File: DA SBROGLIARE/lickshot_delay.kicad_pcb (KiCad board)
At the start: 2 copper layers, 76 parts, among them Q1 2N3904, SW1 SW_DPDT_x2, SW2 SW_DPDT_x2, U1 4069, U2 4046, U3 TL072, U4 L7805, U5 PT2399

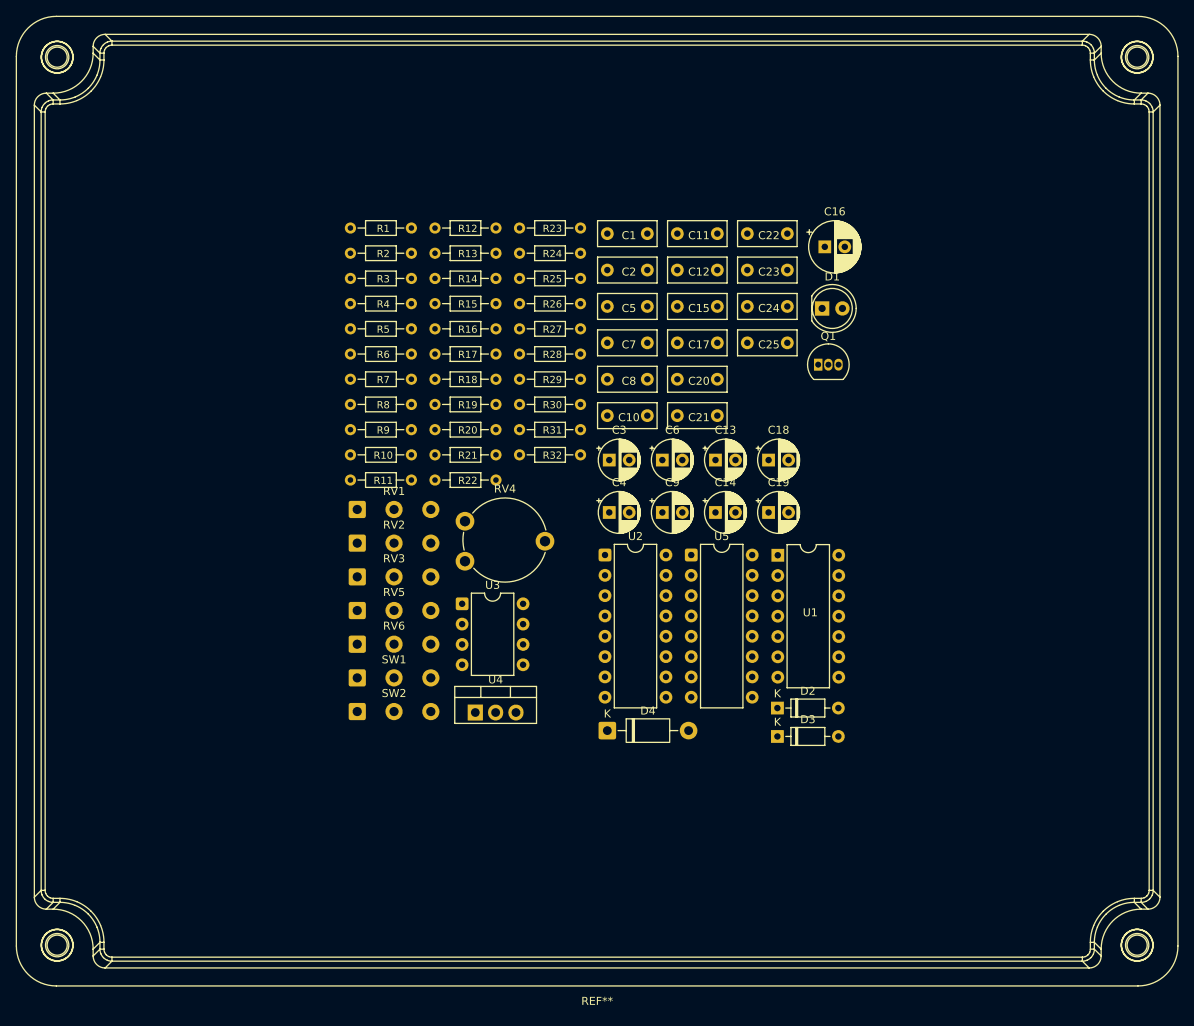
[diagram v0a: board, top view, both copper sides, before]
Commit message: Sbrogliato un po', ho messo i componenti vicino ai IC rispettivi (non ho finito)
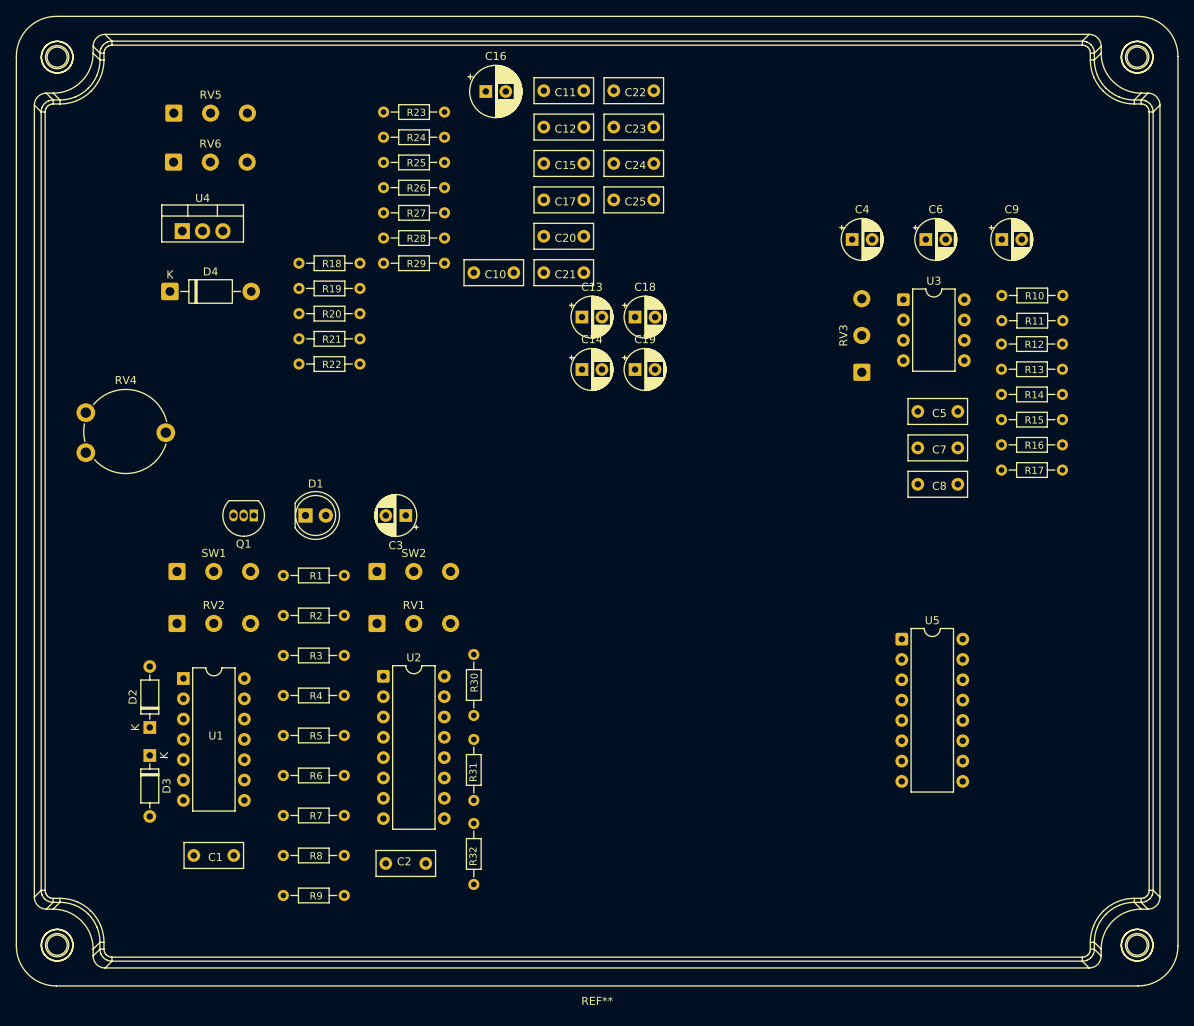
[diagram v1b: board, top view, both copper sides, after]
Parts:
- moved C1 93.3 mm to (71.5, 137.0)
- moved R10 83.8 mm to (172.5, 67.0)
- moved R11 83.8 mm to (172.5, 70.2)
- moved D2 78.5 mm to (66.0, 121.0), turned to 90 degrees
- moved D3 78.5 mm to (66.0, 124.5), turned to -90 degrees
- moved C2 77.6 mm to (100.5, 138.0), turned to 180 degrees
- moved D4 77.5 mm to (68.5, 66.5)
- moved U1 75.9 mm to (70.2, 114.9)
- moved Q1 73.0 mm to (79.0, 94.5), turned to 180 degrees
- moved R12 72.3 mm to (172.5, 73.1)
- moved R13 72.3 mm to (172.5, 76.2)
- moved R14 72.3 mm to (172.5, 79.4)
- moved R15 72.3 mm to (172.5, 82.5)
- moved R16 72.3 mm to (172.5, 85.7)
- moved R17 72.3 mm to (172.5, 88.8)
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
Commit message: Ordinati tutti i componenti, mancano da fare le tracce
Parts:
- removed REF**: Hammond_1590XX, whbeers enclosure_kicad_footprints main Enclosures:Hammond_1590XX
- added J1: Conn_01x02, Connector_Wire:SolderWire-0.5sqmm_1x02_P4.6mm_D0.9mm_OD2.1mm, F.Cu at (179.1, 103.9)
- added J2: 9v, Connector_Wire:SolderWire-0.5sqmm_1x02_P4.6mm_D0.9mm_OD2.1mm, F.Cu at (119.4, 77.5)
- added SW3: SW_SPST, Connector_Wire:SolderWire-0.5sqmm_1x02_P4.6mm_D0.9mm_OD2.1mm, F.Cu at (122.2, 120.7)
- C10: value 47nf -> 4.7n
- C16: footprint Monkey_Riot_Pedals_Library:CP_Electro_D6.3mm_P2.50mm -> Monkey_Riot_Pedals_Library:CP_Electro_Radial_D5.0mm_P2.50mm
- D4: footprint Diode_THT:D_DO-41_SOD81_P10.16mm_Horizontal -> Monkey_Riot_Pedals_Library:DIODE_DO-35_SOD27_P7.62mm_Horizontal
- moved RV4 124.3 mm to (177.9, 119.2), turned to 90 degrees
- moved RV6 103.6 mm to (171.0, 68.6), turned to 180 degrees
- moved R19 96.1 mm to (179.1, 83.8), turned to 90 degrees
- moved R23 95.8 mm to (147.3, 124.5)
- moved R24 84.4 mm to (168.9, 88.3)
- moved R26 82.4 mm to (166.3, 95.2), turned to 180 degrees
- moved R18 82.4 mm to (166.3, 73.7), turned to 180 degrees
- moved R20 82.0 mm to (166.3, 76.2), turned to 180 degrees
- moved RV5 76.3 mm to (141.3, 68.6), turned to 180 degrees
- moved R22 74.1 mm to (158.7, 78.7)
- moved R28 73.1 mm to (141.0, 116.8), turned to 180 degrees
- moved R25 70.6 mm to (158.7, 81.3)
- moved R27 69.0 mm to (158.7, 83.8)
- moved C22 68.1 mm to (170.2, 91.4)
- moved U4 67.8 mm to (129.5, 91.4), turned to 90 degrees
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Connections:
- C5 pad 1: Net-(C5-Pad1) -> Net-(SW3-B)
- D4 pad 2: +9V -> Net-(D4-A)
- R10 pad 1: unconnected-(R10-Pad1) -> Net-(J1-Pin_1)
- R14 pad 2: Net-(C5-Pad1) -> Net-(SW3-B)
- R8 pad 1: Net-(C5-Pad1) -> Net-(SW3-A)
- R9 pad 2: Net-(C5-Pad1) -> Net-(SW3-A)
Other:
- board text added: "9V"
- board text added: "gnd"
- board text added: "out"

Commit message: finita
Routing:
- net VCC: track 0.00 -> 134.8 mm
- net VREF: track 0.00 -> 56.2 mm
- net Net-(C10-Pad1): track 0.00 -> 55.3 mm
- net Net-(SW1A-B): track 0.00 -> 53.7 mm
- net Net-(D2-K): track 0.00 -> 44.3 mm
- net Net-(C6-Pad1): track 0.00 -> 39.3 mm
- net Net-(R19-Pad1): track 0.00 -> 39.1 mm
- net Net-(Q1-B): track 0.00 -> 33.7 mm
- net Net-(C6-Pad2): track 0.00 -> 31.4 mm
- net Net-(U2-R1): track 0.00 -> 31.1 mm
- net Net-(R6-Pad2): track 0.00 -> 31.1 mm
- net Net-(SW3-A): track 0.00 -> 30.4 mm
- net Net-(C22-Pad1): track 0.00 -> 29.9 mm
- net Net-(C11-Pad1): track 0.00 -> 28.7 mm
- net Net-(U2-FOUT): track 0.00 -> 28.5 mm
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- added copper zone on B.Cu, net GND
- added copper zone on F.Cu, net GND
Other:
- board outline added: 99.1 x 63.5 mm
- board text added: "Lickshot V.1"
- board text added: "Roots Music Against Fascism"
